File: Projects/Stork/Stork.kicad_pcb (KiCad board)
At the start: 4 copper layers, 200 x 100 mm, 559 parts, among them J25 Conn_02x03_Odd_Even, J26 Conn_01x03_Male, J27 Screw_Terminal_01x02, J28 Conn_01x03_Male, J29 Conn_01x03_Male, J30 Conn_01x03_Male, J31 Conn_02x05_Top_Bottom, J32 Conn_02x05_Top_Bottom, J33 Conn_02x05_Top_Bottom, J34 Conn_02x05_Top_Bottom, J35 Conn_02x05_Top_Bottom, J36 Conn_02x05_Top_Bottom, J37 Conn_02x05_Top_Bottom, J38 Conn_02x05_Top_Bottom, J39 Conn_02x05_Top_Bottom, J40 Conn_02x05_Top_Bottom, J41 Conn_02x05_Top_Bottom, J42 Conn_02x05_Top_Bottom, U1 AD7991YRJZ-1500RL7, U10 AD8608ARZ-SOIC127P600X175-14N, U11 AD7991YRJZ-1500RL7, U12 AD8608ARZ-SOIC127P600X175-14N, U13 AD7991YRJZ-1500RL7, U14 AD8608ARZ-SOIC127P600X175-14N, U15 AD7991YRJZ-1500RL7, U16 AD8608ARZ-SOIC127P600X175-14N, U17 AD7991YRJZ-1500RL7, U18 AD8608ARZ-SOIC127P600X175-14N, U19 AD7991YRJZ-1500RL7, U2 AD8608ARZ-SOIC127P600X175-14N, U20 AD8608ARZ-SOIC127P600X175-14N, U21 AD7991YRJZ-1500RL7, U22 AD8608ARZ-SOIC127P600X175-14N, U23 AD7991YRJZ-1500RL7, U24 AD8608ARZ-SOIC127P600X175-14N, U25 AD7991YRJZ-1500RL7, U26 AD8608ARZ-SOIC127P600X175-14N, U27 AD7991YRJZ-1500RL7, U28 AD8608ARZ-SOIC127P600X175-14N, U29 AD7991YRJZ-1500RL7, U3 AD7991YRJZ-1500RL7, U30 AD8608ARZ-SOIC127P600X175-14N, U31 AD7991YRJZ-1500RL7, U32 AD8608ARZ-SOIC127P600X175-14N, U33 Digilent-CoraZ7, U34 AD7991YRJZ-1500RL7, U35 AD8608ARZ-SOIC127P600X175-14N, U36 AD7991YRJZ-1500RL7, U37 AD8608ARZ-SOIC127P600X175-14N, U38 AD7991YRJZ-1500RL7, U39 AD8608ARZ-SOIC127P600X175-14N, U4 AD8608ARZ-SOIC127P600X175-14N, U40 AD7991YRJZ-1500RL7, U41 AD8608ARZ-SOIC127P600X175-14N, U42 AD7991YRJZ-1500RL7, U43 AD8608ARZ-SOIC127P600X175-14N, U44 AD7991YRJZ-1500RL7, U45 AD8608ARZ-SOIC127P600X175-14N, U46 AD7991YRJZ-1500RL7, U47 AD8608ARZ-SOIC127P600X175-14N, U48 AD7991YRJZ-1500RL7, U49 AD8608ARZ-SOIC127P600X175-14N, U5 AD7991YRJZ-1500RL7, U50 TPS79330-EP, U51 TPS73150DBV, U6 AD8608ARZ-SOIC127P600X175-14N, U7 AD7991YRJZ-1500RL7, U8 AD8608ARZ-SOIC127P600X175-14N, U9 AD7991YRJZ-1500RL7

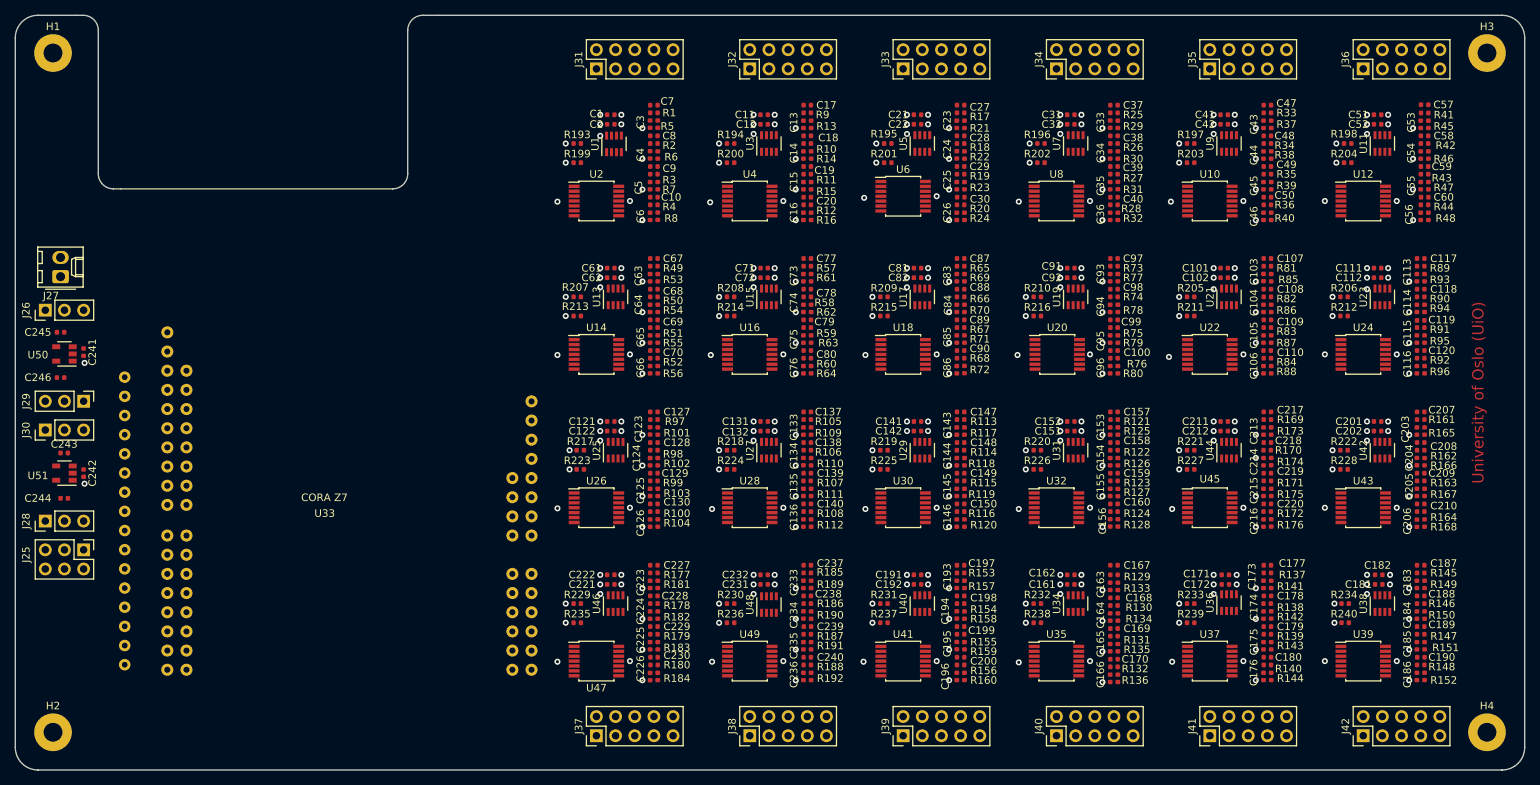
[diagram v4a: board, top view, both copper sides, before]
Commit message: added vdd_filter tracks manually on power plane
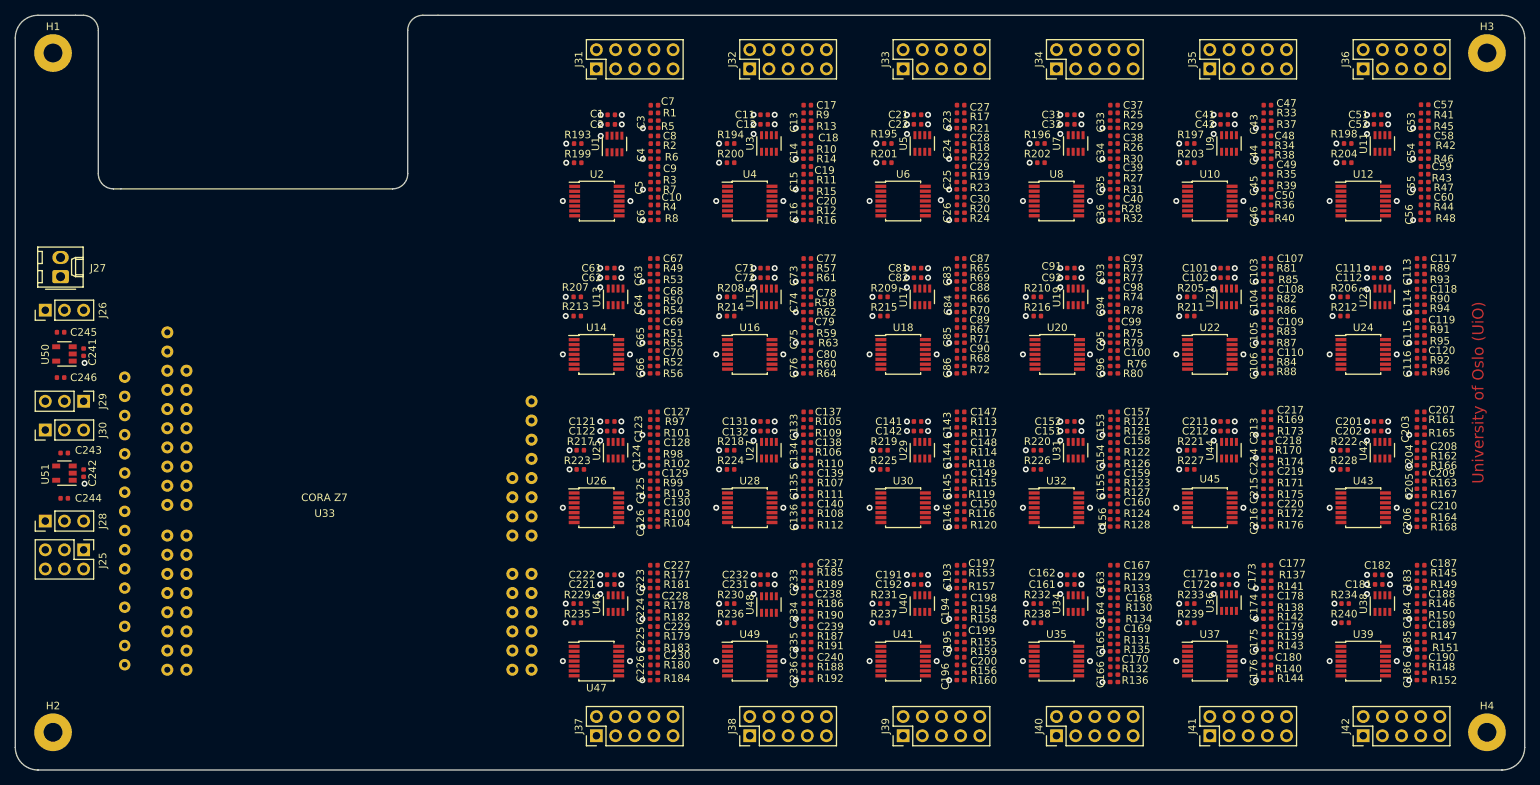
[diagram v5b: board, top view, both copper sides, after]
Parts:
- moved U6 0.64 mm to (167.6, 54.6)
- moved R5 0.06 mm to (135.2, 44.4)
- moved R6 0.06 mm to (135.2, 48.5)
- moved R7 0.06 mm to (135.2, 52.6)
- moved R8 0.06 mm to (135.2, 56.6)
- moved R193 0.06 mm to (124.5, 47.0)
- moved R199 0.06 mm to (124.5, 49.5)
- moved C10 0.06 mm to (134.7, 54.1)
- moved C7 0.06 mm to (134.7, 41.9)
- moved C8 0.06 mm to (134.7, 46.0)
- moved C9 0.06 mm to (134.7, 50.0)
- moved U1 0.06 mm to (129.4, 47.1)
- moved C1 0.06 mm to (129.0, 43.2)
- moved C2 0.06 mm to (129.0, 44.5)
- moved C3 0.06 mm to (134.2, 44.4)
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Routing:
- net VDD_Filters: track 0.00 -> 603.4 mm, vias 13 -> 24
- net SDA18: vias 2 -> 0
- net SCL19: vias 1 -> 0
- net SCL15: vias 1 -> 0
- net GND: vias 166 -> 170
- net 3V3_CoraZ7: vias 2 -> 0
- net +3V3: vias 123 -> 114
